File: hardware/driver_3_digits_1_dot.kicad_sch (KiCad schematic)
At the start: 12 parts, among them U4 HV5622PG

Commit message: Remove HV capacitor for Nixies. Add more LCSC references.
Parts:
- removed C10: C, Capacitor_SMD:C_1206_3216Metric, symbol Device:C
- C9: value C -> 100nF
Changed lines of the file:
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@@
-	)
-	(junction
-		(at 182.88 82.55)
-		(diameter 0)
-		(color 0 0 0 0)
 	)
 	(junction
@@
 		(pts
 			(xy 88.9 46.99) (xy 121.92 46.99)
-		)
-		(stroke
-			(width 0)
-			(type default)
-		)
-	)
-	(wire
-		(pts
-			(xy 182.88 90.17) (xy 182.88 93.98)
 		)
 		(stroke
@@
 			)
 			(justify left)
-		)
-	)
-	(hierarchical_label "GND"
-		(shape input)
-		(at 182.88 93.98 270)
-		(effects
-			(font
-				(size 1.27 1.27)
-			)
-			(justify right)
 		)
 	)
@@
 	(symbol
 		(lib_id "Device:C")
-		(at 182.88 86.36 0)
-		(unit 1)
-		(exclude_from_sim no)
-		(in_bom yes)
-		(on_board yes)
-		(dnp no)
-		(fields_autoplaced yes)
-		(property "Reference" "C10"
-			(at 186.69 85.0899 0)
-			(effects
-				(font
-					(size 1.27 1.27)
-				)
-				(justify left)
-			)
-		)
-		(property "Value" "C"
-			(at 186.69 87.6299 0)
-			(effects
-				(font
-					(size 1.27 1.27)
-				)
-				(justify left)
-			)
-		)
-		(property "Footprint" "Capacitor_SMD:C_1206_3216Metric"
-			(at 183.8452 90.17 0)
-			(effects
-				(font
-					(size 1.27 1.27)
-				)
-				(hide yes)
-			)
-		)
-		(property "Datasheet" "~"
-			(at 182.88 86.36 0)
-			(effects
-				(font
-					(size 1.27 1.27)
-				)
-				(hide yes)
-			)
-		)
-		(property "Description" "Unpolarized capacitor"
-			(at 182.88 86.36 0)
-			(effects
-				(font
-					(size 1.27 1.27)
-				)
-				(hide yes)
-			)
-		)
-		(pin "2"
-		)
-		(pin "1"
-		)
-		(instances
-			(project ""
-				(path "/90430e5f-7049-4de8-b92d-f897c4a89819/4b7e288e-9913-4bd2-a435-f0a0986d442d"
-					(reference "C10")
-					(unit 1)
-				)
-			)
-		)
-	)
-	(symbol
-		(lib_id "Device:C")
 		(at 121.92 152.4 180)
 		(unit 1)
@@
 			)
 		)
-		(property "Value" "C"
+		(property "Value" "100nF"
 			(at 125.73 153.6699 0)
 			(effects

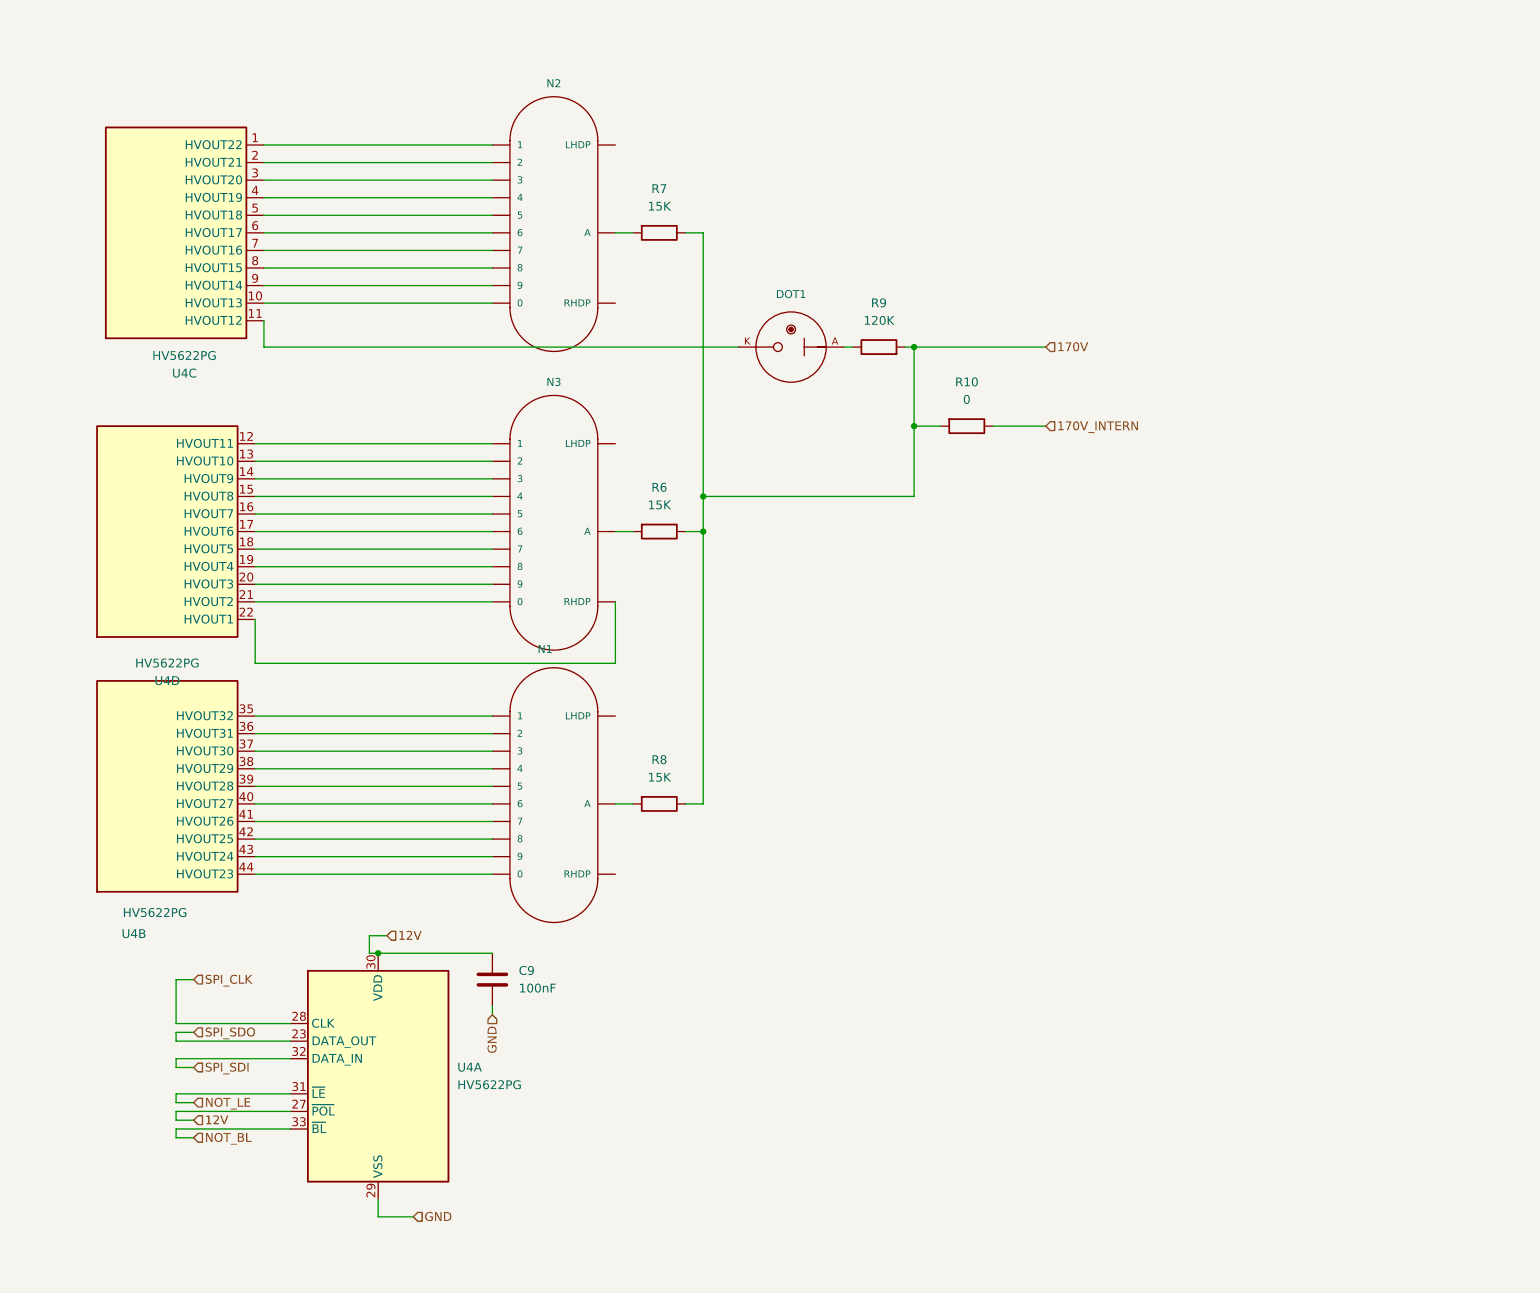
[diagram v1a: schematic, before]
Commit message: Add mosfets for handling levels.
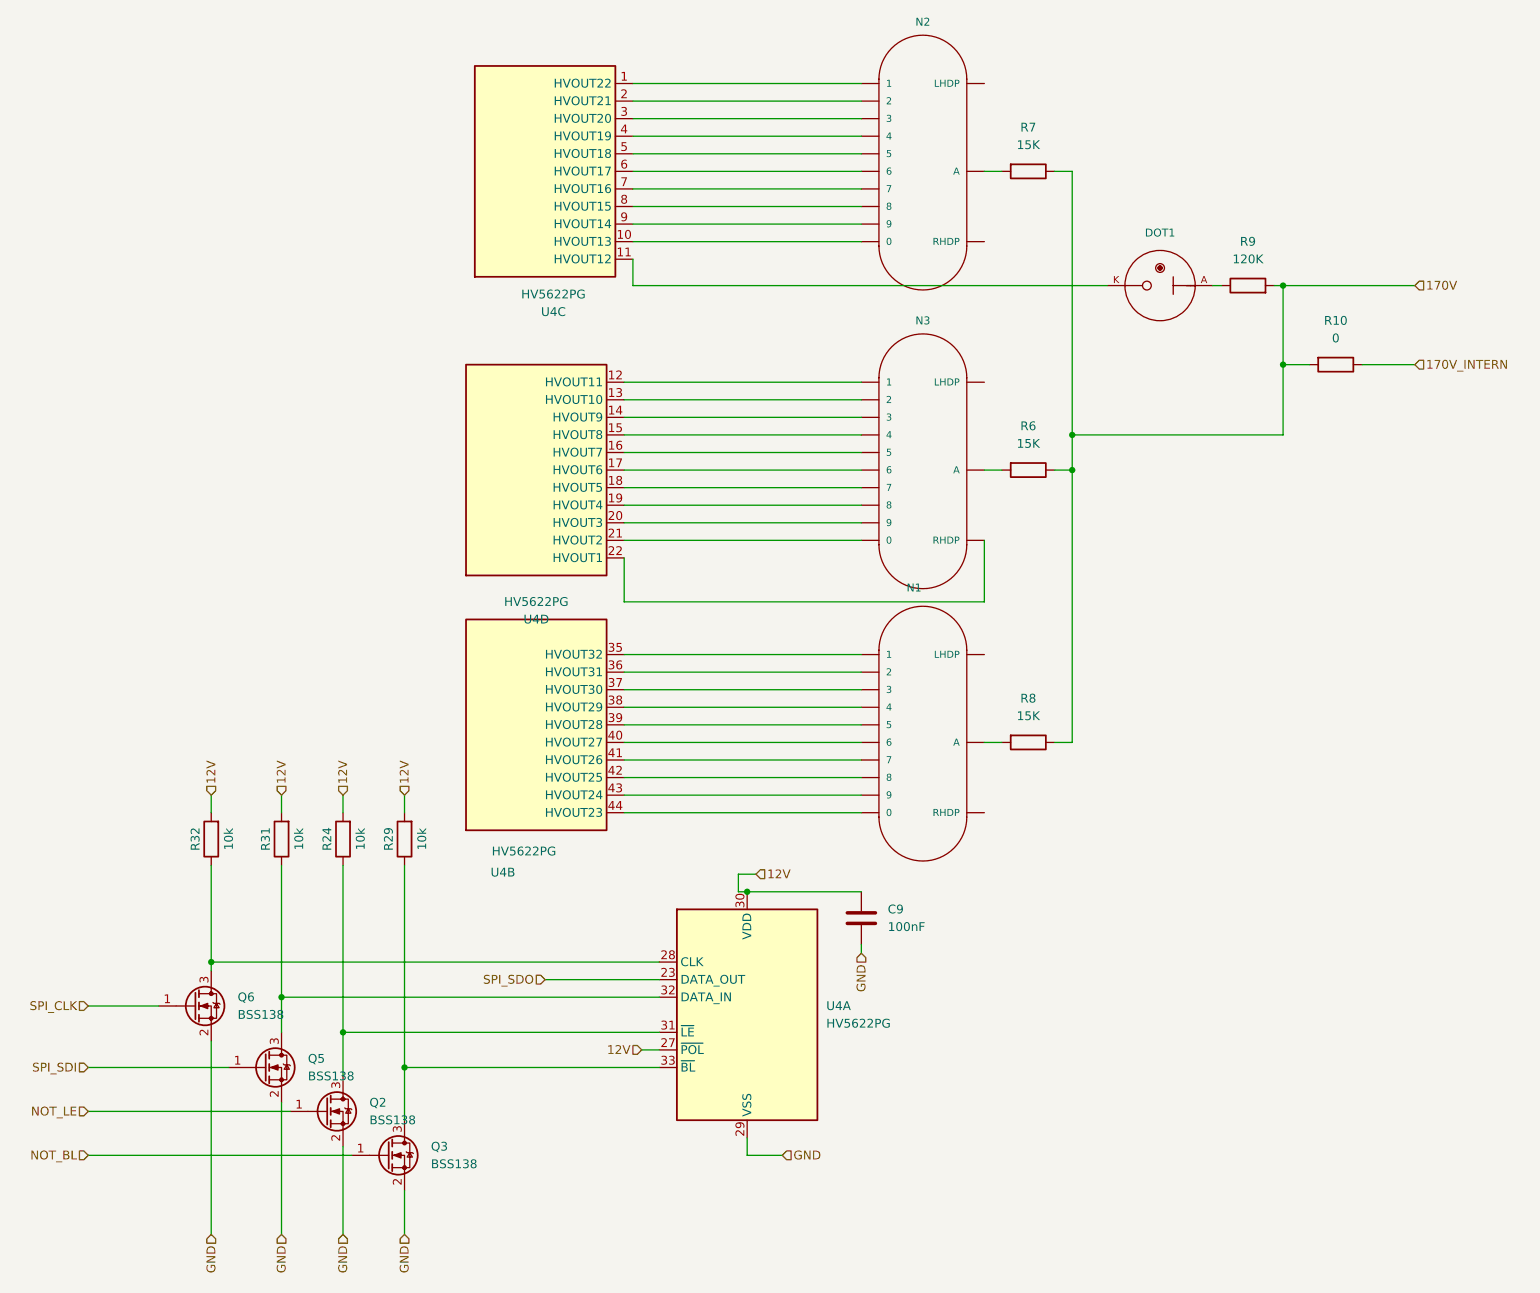
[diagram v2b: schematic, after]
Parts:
- added Q2, Q3, Q5, Q6: BSS138, Package_TO_SOT_SMD:SOT-23, symbol Transistor_FET:BSS138
- added R24, R29, R31, R32: 10k, Resistor_SMD:R_0805_2012Metric, symbol Device:R
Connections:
- net 12V: now also R24.2, R29.2, R31.2, R32.2
- net GND: now also Q2.2 (S), Q3.2 (S), Q5.2 (S), Q6.2 (S)
- net NOT_BL: now also Q3.1 (G); no longer U4.33 (~{BL})
- net NOT_LE: now also Q2.1 (G); no longer U4.31 (~{LE})
- net SPI_CLK: now also Q6.1 (G); no longer U4.28 (CLK)
- net SPI_SDI: now also Q5.1 (G); no longer U4.32 (DATA_IN)
- new net: Q3.3 (D), R29.1, U4.33 (~{BL})
- new net: Q5.3 (D), R31.1, U4.32 (DATA_IN)
- new net: Q2.3 (D), R24.1, U4.31 (~{LE})
- new net: Q6.3 (D), R32.1, U4.28 (CLK)
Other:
- moved on the sheet: C9, DOT1, N1, N2, N3, R10, R6, R7, R8, R9, U4A, U4B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
